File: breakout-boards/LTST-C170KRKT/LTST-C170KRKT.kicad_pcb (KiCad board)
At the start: 2 copper layers, 14 parts, among them J1 Conn_01x12, J2 Conn_01x12

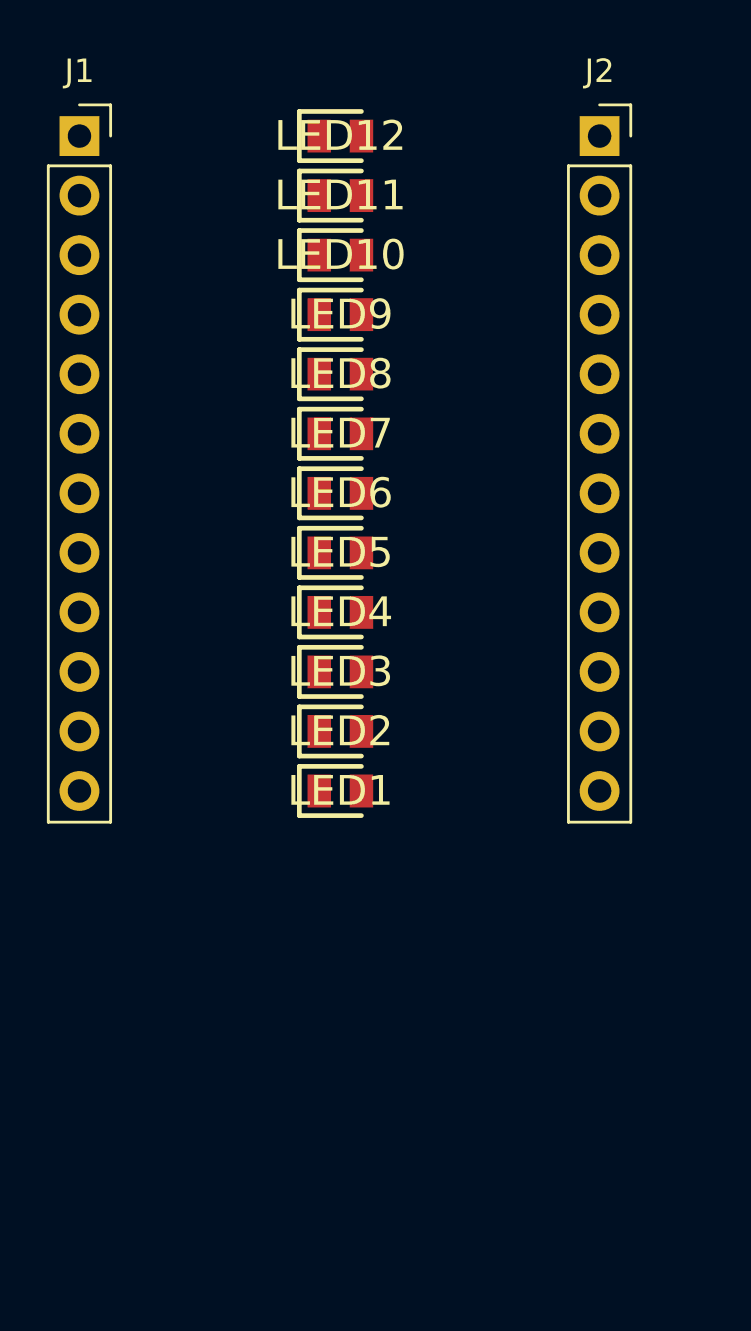
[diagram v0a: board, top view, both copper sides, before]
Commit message: feat: create footprint for LED breakout board
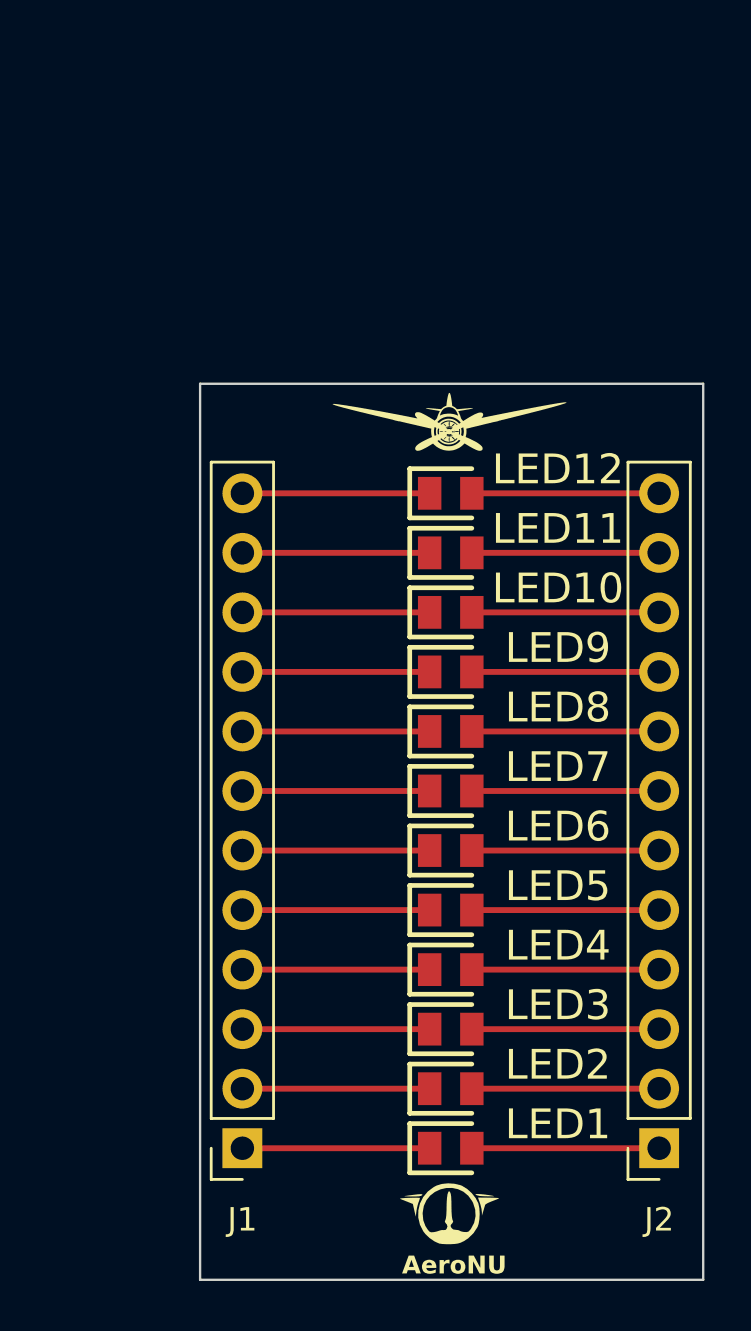
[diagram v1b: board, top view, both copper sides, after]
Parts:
- added AeroNU: LOGO, FixedWing:AeroNU - Logo (Smol), F.Cu at (161.4, 109.7)
- added FixedWing: LOGO, FixedWing:FixedWing - Logo (Smol), F.Cu at (161.3, 73.8)
- moved J1 43.7 mm to (152.4, 104.1), turned to 180 degrees
- moved J2 43.3 mm to (170.2, 104.1), turned to 180 degrees
- moved LED3 16.0 mm to (161.3, 99.1)
- moved LED5 16.0 mm to (161.3, 94.0)
- moved LED7 16.0 mm to (161.3, 88.9)
- moved LED12 16.0 mm to (161.3, 76.2)
- moved LED1 16.0 mm to (161.3, 104.1)
- moved LED10 16.0 mm to (161.3, 81.3)
- moved LED11 16.0 mm to (161.3, 78.7)
- moved LED2 16.0 mm to (161.3, 101.6)
- moved LED4 16.0 mm to (161.3, 96.5)
- moved LED6 16.0 mm to (161.3, 91.4)
- moved LED8 16.0 mm to (161.3, 86.4)
- moved LED9 16.0 mm to (161.3, 83.8)
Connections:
- LED1 pad 1: Net-(J1-Pin_12) -> Net-(J1-Pin_1)
- LED1 pad 2: Net-(J2-Pin_12) -> Net-(J2-Pin_1)
- LED10 pad 1: Net-(J1-Pin_3) -> Net-(J1-Pin_10)
- LED10 pad 2: Net-(J2-Pin_3) -> Net-(J2-Pin_10)
- LED11 pad 1: Net-(J1-Pin_2) -> Net-(J1-Pin_11)
- LED11 pad 2: Net-(J2-Pin_2) -> Net-(J2-Pin_11)
- LED12 pad 1: Net-(J1-Pin_1) -> Net-(J1-Pin_12)
- LED12 pad 2: Net-(J2-Pin_1) -> Net-(J2-Pin_12)
- LED2 pad 1: Net-(J1-Pin_11) -> Net-(J1-Pin_2)
- LED2 pad 2: Net-(J2-Pin_11) -> Net-(J2-Pin_2)
- LED3 pad 1: Net-(J1-Pin_10) -> Net-(J1-Pin_3)
- LED3 pad 2: Net-(J2-Pin_10) -> Net-(J2-Pin_3)
- LED4 pad 1: Net-(J1-Pin_9) -> Net-(J1-Pin_4)
- LED4 pad 2: Net-(J2-Pin_9) -> Net-(J2-Pin_4)
- LED5 pad 1: Net-(J1-Pin_8) -> Net-(J1-Pin_5)
- LED5 pad 2: Net-(J2-Pin_8) -> Net-(J2-Pin_5)
- LED6 pad 1: Net-(J1-Pin_7) -> Net-(J1-Pin_6)
- LED6 pad 2: Net-(J2-Pin_7) -> Net-(J2-Pin_6)
- LED7 pad 1: Net-(J1-Pin_6) -> Net-(J1-Pin_7)
- LED7 pad 2: Net-(J2-Pin_6) -> Net-(J2-Pin_7)
- LED8 pad 1: Net-(J1-Pin_5) -> Net-(J1-Pin_8)
- LED8 pad 2: Net-(J2-Pin_5) -> Net-(J2-Pin_8)
- LED9 pad 1: Net-(J1-Pin_4) -> Net-(J1-Pin_9)
- LED9 pad 2: Net-(J2-Pin_4) -> Net-(J2-Pin_9)
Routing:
- net Net-(J2-Pin_9): track 0.00 -> 7.99 mm
- net Net-(J2-Pin_8): track 0.00 -> 7.99 mm
- net Net-(J2-Pin_7): track 0.00 -> 7.99 mm
- net Net-(J2-Pin_6): track 0.00 -> 7.99 mm
- net Net-(J2-Pin_5): track 0.00 -> 7.99 mm
- net Net-(J2-Pin_4): track 0.00 -> 7.99 mm
- net Net-(J2-Pin_3): track 0.00 -> 7.99 mm
- net Net-(J2-Pin_2): track 0.00 -> 7.99 mm
- net Net-(J2-Pin_12): track 0.00 -> 7.99 mm
- net Net-(J2-Pin_11): track 0.00 -> 7.99 mm
- net Net-(J2-Pin_10): track 0.00 -> 7.99 mm
- net Net-(J2-Pin_1): track 0.00 -> 7.99 mm
- net Net-(J1-Pin_9): track 0.00 -> 7.99 mm
- net Net-(J1-Pin_8): track 0.00 -> 7.99 mm
- net Net-(J1-Pin_7): track 0.00 -> 7.99 mm
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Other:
- board outline added: 21.5 x 38.2 mm
- board text added: "AeroNU"
- board text added: "Designed By Ephram CJ and Matthew F"

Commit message: feat: finalize LED board design
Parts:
- moved LED1 4.32 mm to (165.6, 104.1)
- moved LED10 4.32 mm to (165.6, 81.3)
- moved LED4 4.32 mm to (165.6, 96.5)
- moved LED7 4.32 mm to (165.6, 88.9)
- moved LED12 4.32 mm to (157.0, 76.2)
- moved LED3 4.32 mm to (157.0, 99.1)
- moved LED6 4.32 mm to (157.0, 91.4)
- moved LED9 4.32 mm to (157.0, 83.8)
- moved FixedWing 4.19 mm to (165.4, 73.2)
- moved AeroNU 3.99 mm to (157.4, 109.4)
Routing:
- net Net-(J2-Pin_7): track 7.99 -> 3.67 mm
- net Net-(J2-Pin_4): track 7.99 -> 3.67 mm
- net Net-(J2-Pin_10): track 7.99 -> 3.67 mm
- net Net-(J2-Pin_1): track 7.99 -> 3.67 mm
- net Net-(J1-Pin_7): track 7.99 -> 12.3 mm
- net Net-(J1-Pin_4): track 7.99 -> 12.3 mm
- net Net-(J1-Pin_10): track 7.99 -> 12.3 mm
- net Net-(J1-Pin_1): track 7.99 -> 12.3 mm
- net Net-(J2-Pin_9): track 7.99 -> 12.3 mm
- net Net-(J2-Pin_6): track 7.99 -> 12.3 mm
- net Net-(J2-Pin_3): track 7.99 -> 12.3 mm
- net Net-(J2-Pin_12): track 7.99 -> 12.3 mm
- net Net-(J1-Pin_9): track 7.99 -> 3.67 mm
- net Net-(J1-Pin_6): track 7.99 -> 3.67 mm
- net Net-(J1-Pin_3): track 7.99 -> 3.67 mm
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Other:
- board size 21.5 x 38.2 mm -> 21.5 x 38.7 mm

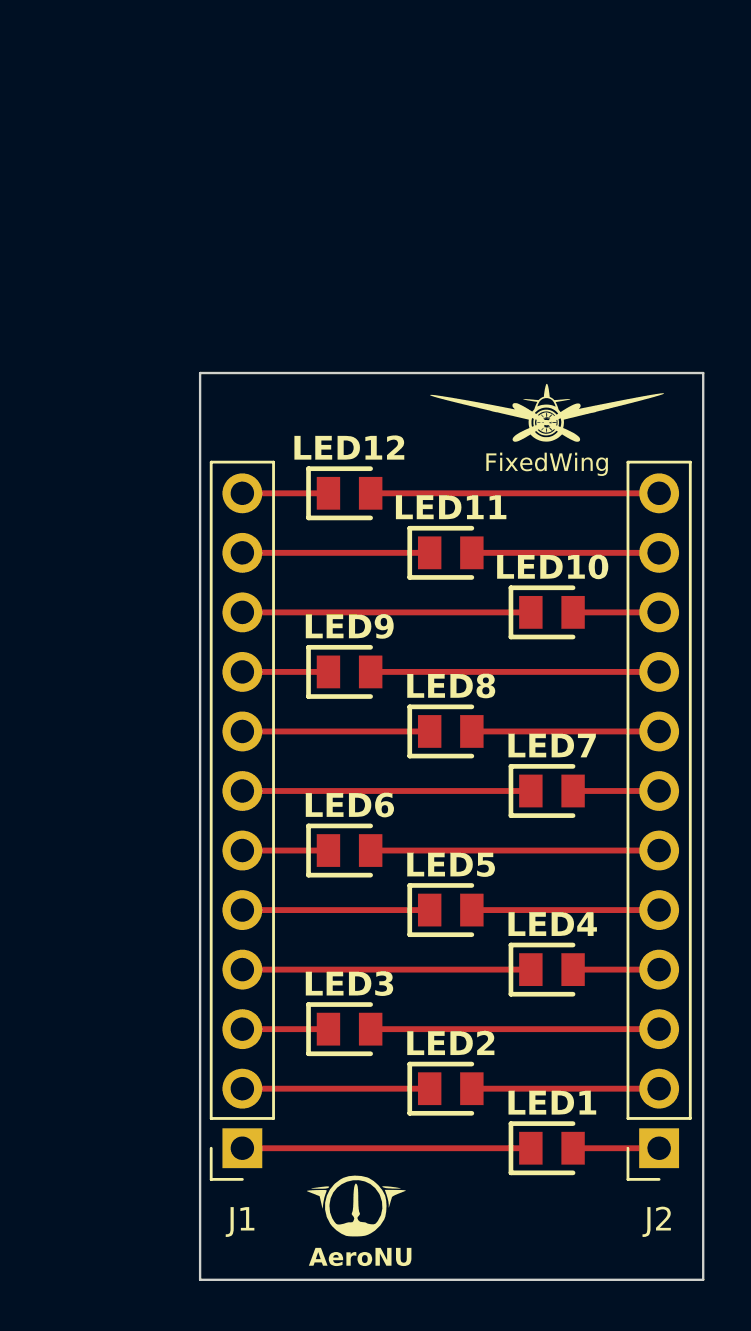
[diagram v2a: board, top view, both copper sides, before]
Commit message: feat: add fillets to all boards
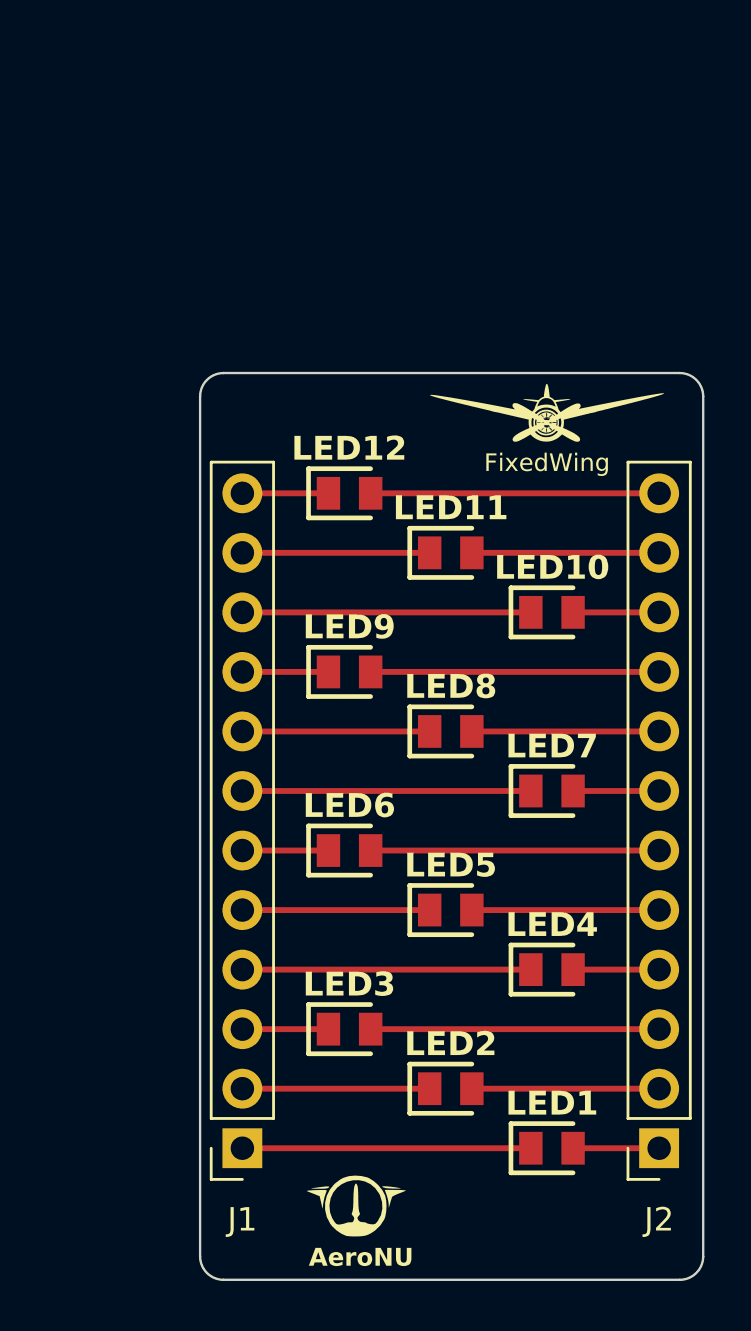
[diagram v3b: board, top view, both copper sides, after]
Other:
- outline, holes or cut-outs redrawn
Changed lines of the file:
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@@
       (outputformat 1)
       (mirror false)
-      (drillshape 1)
+      (drillshape 0)
       (scaleselection 1)
       (outputdirectory "")
@@
     )
   )
-  (gr_rect (start 150.5966 71.0692) (end 172.0596 109.7534)
-    (stroke (width 0.1) (type default)) (fill none) (layer "Edge.Cuts"))
+  (gr_line (start 171.0596 109.7534) (end 151.5966 109.7534)
+    (stroke (width 0.1) (type default)) (layer "Edge.Cuts"))
+  (gr_line (start 172.0596 72.0692) (end 172.0596 108.7534)
+    (stroke (width 0.1) (type default)) (layer "Edge.Cuts"))
+  (gr_line (start 151.5966 71.0692) (end 171.0596 71.0692)
+    (stroke (width 0.1) (type default)) (layer "Edge.Cuts"))
+  (gr_line (start 150.5966 108.7534) (end 150.5966 72.0692)
+    (stroke (width 0.1) (type default)) (layer "Edge.Cuts"))
+  (gr_arc (start 151.5966 109.7534) (mid 150.889493 109.460507) (end 150.5966 108.7534)
+    (stroke (width 0.1) (type default)) (layer "Edge.Cuts"))
+  (gr_arc (start 171.0596 71.0692) (mid 171.766707 71.362093) (end 172.0596 72.0692)
+    (stroke (width 0.1) (type default)) (layer "Edge.Cuts"))
+  (gr_arc (start 150.5966 72.0692) (mid 150.889493 71.362093) (end 151.5966 71.0692)
+    (stroke (width 0.1) (type default)) (layer "Edge.Cuts"))
+  (gr_arc (start 172.0596 108.7534) (mid 171.766707 109.460507) (end 171.0596 109.7534)
+    (stroke (width 0.1) (type default)) (layer "Edge.Cuts"))
   (gr_text "Designed By\nEphram CJ and Matthew F" (at 161.3408 108.6104) (layer "B.SilkS")
     (effects (font (size 0.762 0.762) (thickness 0.127) bold) (justify bottom mirror))
